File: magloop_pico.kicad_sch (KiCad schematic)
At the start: 102 parts, among them J1 Conn_Coaxial_Power, J10 5V AUDIO MUTE, J2 Conn_02x03_Odd_Even, J3 POWER SW, J4 Conn_02x03_Odd_Even, J5 Conn_02x04_Odd_Even, J6 TO RF RELAY, J7 ETHERNET, J8 5-1634513-1, J9 12V AUDIO MUTE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

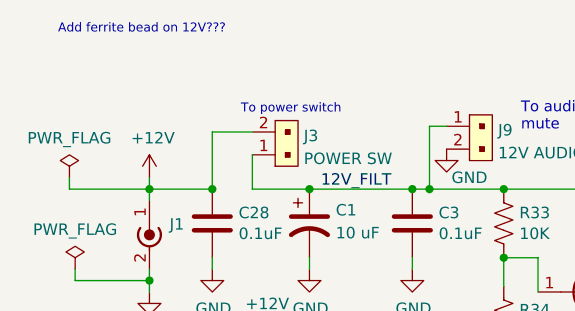
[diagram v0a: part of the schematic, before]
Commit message: Added BOM directory
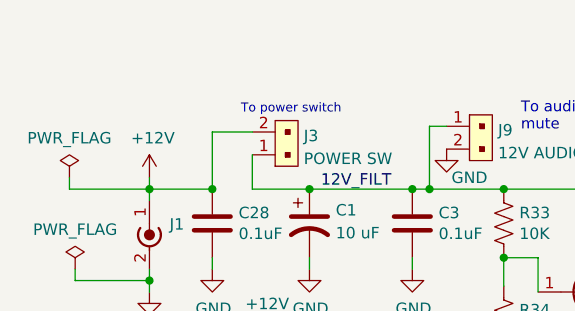
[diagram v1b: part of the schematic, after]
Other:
- note removed: "Add ferrite bead on 12V???"
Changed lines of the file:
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@@
     (effects (font (size 2.0066 2.0066)) (justify left bottom))
-  )
-  (text "Add ferrite bead on 12V???" (at 16.51 5.715 0)
-    (effects (font (size 1 1)) (justify left bottom))
   )
   (text "RF bypasses or ferrite beads for stepper outs?" (at 12.065 192.405 0)

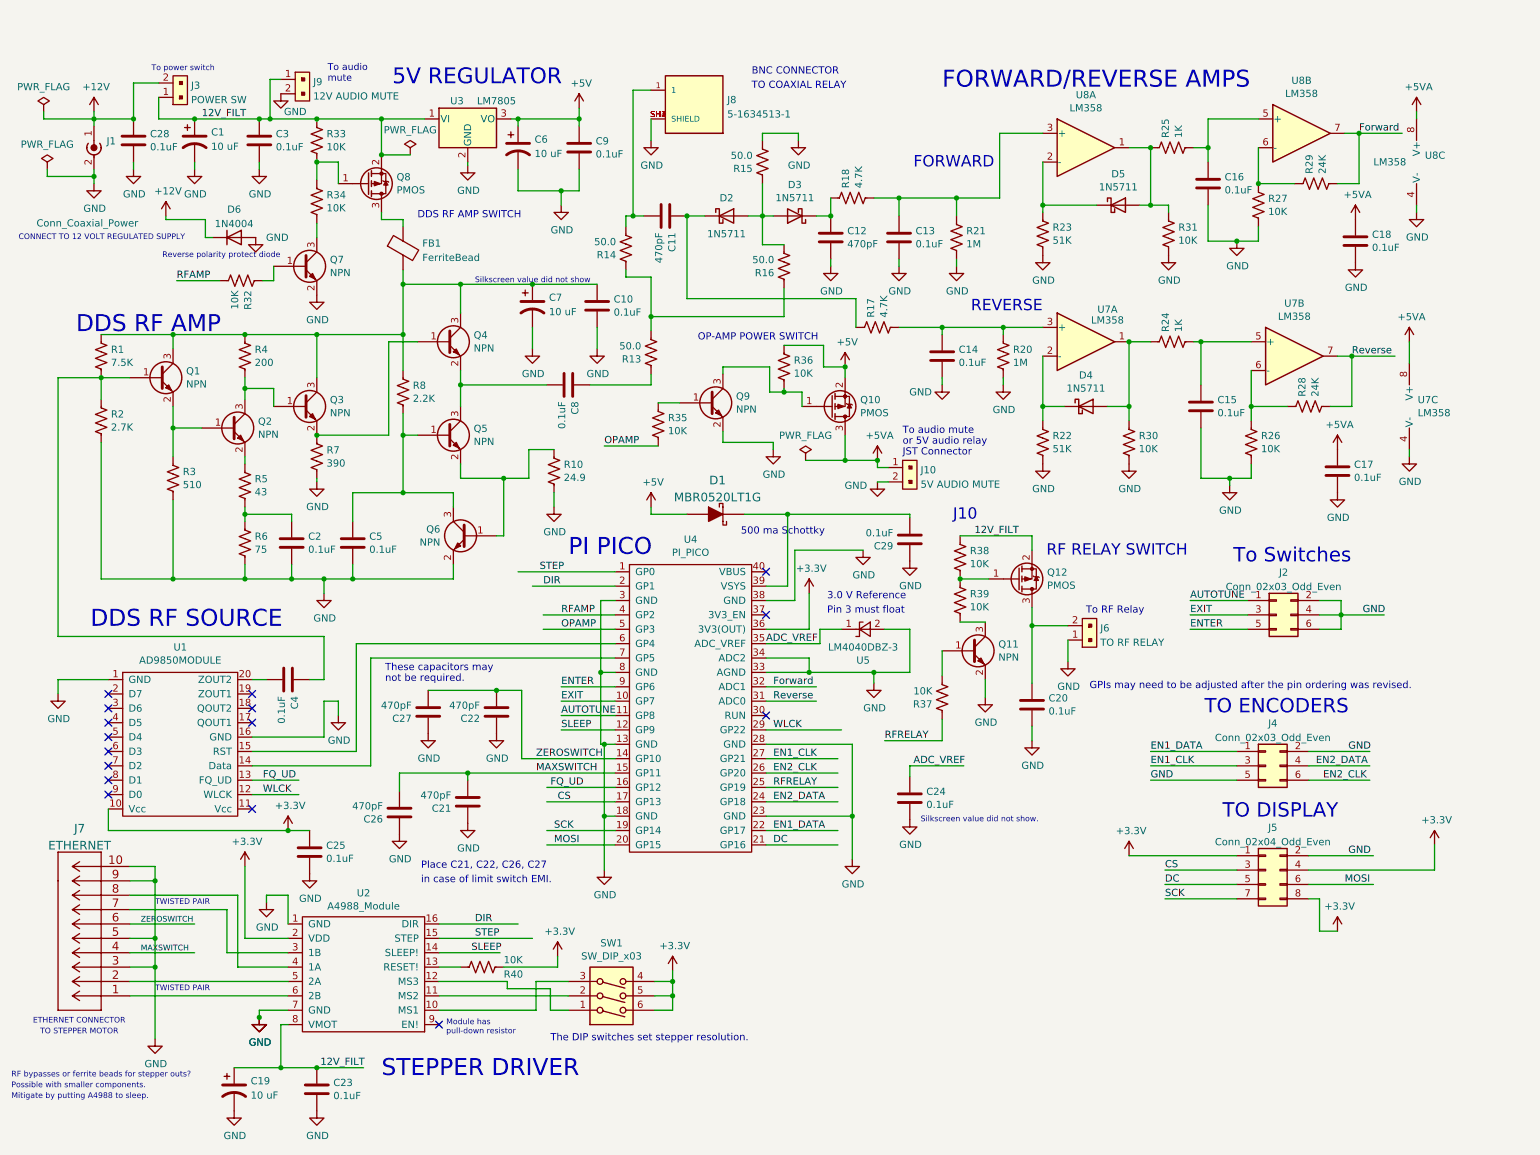
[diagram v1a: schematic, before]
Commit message: Added BOMs from Digikey and Kicad schematic.  Minor clean up top metal and changed 50 ohm resistors to 51.
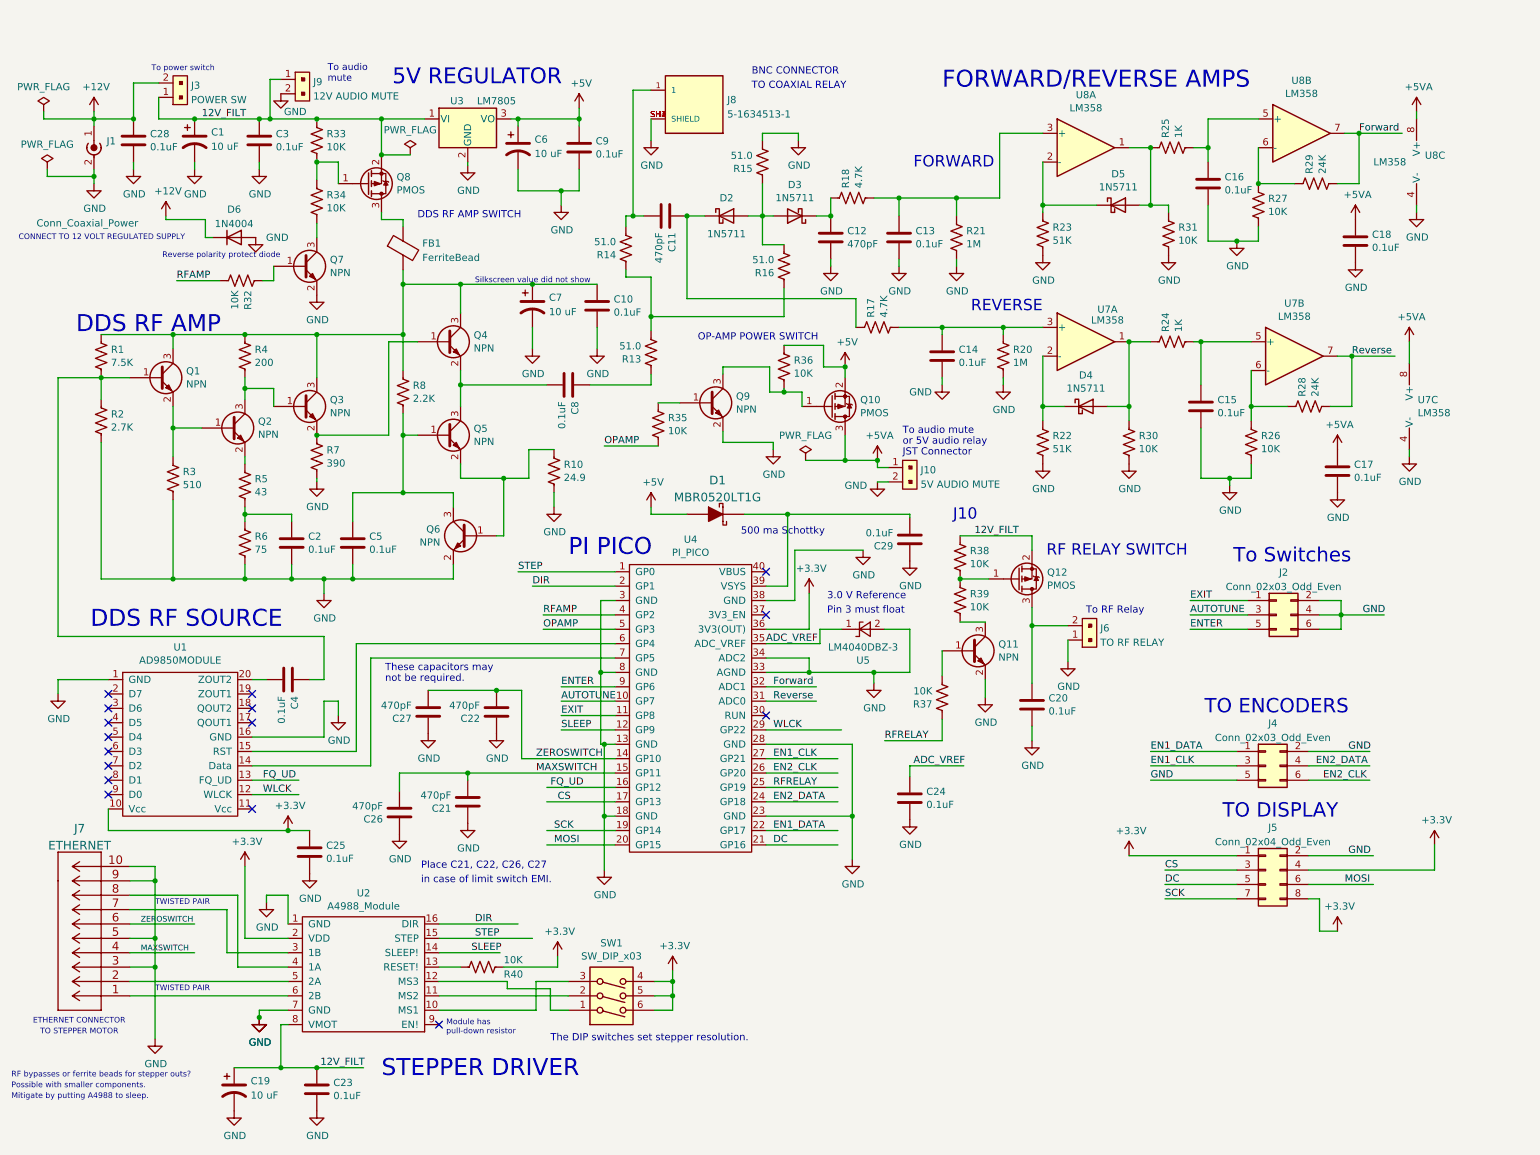
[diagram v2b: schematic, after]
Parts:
- R13, R14, R15, R16: value 50.0 -> 51.0
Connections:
- net AUTOTUNE: now also J2.3 (Pin_3), U4.10 (GP7); no longer J2.1 (Pin_1), U4.11 (GP8)
- net EXIT: now also J2.1 (Pin_1), U4.11 (GP8); no longer J2.3 (Pin_3), U4.10 (GP7)
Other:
- note removed: "GPIs may need to be adjusted after the pin ordering was revised."
- note removed: "Silkscreen value did not show."
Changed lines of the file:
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@@
     (effects (font (size 1.27 1.27)) (justify left bottom))
   )
-  (text "GPIs may need to be adjusted after the pin ordering was revised."
-    (at 202.565 123.825 0)
-    (effects (font (size 1.27 1.27)) (justify left bottom))
-  )
   (text "TWISTED PAIR" (at 37.465 177.165 0)
     (effects (font (size 0.9906 0.9906)) (justify left bottom))
@@
     (effects (font (size 1.27 1.27)) (justify left bottom))
   )
-  (text "Silkscreen value did not show." (at 172.72 147.32 0)
-    (effects (font (size 1 1)) (justify left bottom))
-  )
   (text "TO ENCODERS" (at 222.885 128.27 0)
     (effects (font (size 2.54 2.54)) (justify left bottom))
@@
     (effects (font (size 1.27 1.27)) (justify left bottom))
   )
-  (label "EXIT" (at 109.22 125.73 0)
+  (label "AUTOTUNE" (at 109.22 125.73 0)
     (effects (font (size 1.27 1.27)) (justify left bottom))
   )
@@
     (effects (font (size 1.27 1.27)) (justify left bottom))
   )
-  (label "AUTOTUNE" (at 109.22 128.27 0)
+  (label "EXIT" (at 109.22 128.27 0)
     (effects (font (size 1.27 1.27)) (justify left bottom))
   )
@@
     (effects (font (size 1.27 1.27)) (justify left bottom))
   )
-  (label "STEP" (at 105.41 102.87 0)
+  (label "STEP" (at 101.6 102.87 0)
     (effects (font (size 1.27 1.27)) (justify left bottom))
   )
@@
     (effects (font (size 1.27 1.27)) (justify left bottom))
   )
-  (label "EXIT" (at 220.345 110.49 0)
+  (label "AUTOTUNE" (at 220.345 110.49 0)
     (effects (font (size 1.27 1.27)) (justify left bottom))
   )
@@
     (effects (font (size 1.27 1.27)) (justify left bottom))
   )
-  (label "AUTOTUNE" (at 220.345 107.95 0)
+  (label "EXIT" (at 220.345 107.95 0)
     (effects (font (size 1.27 1.27)) (justify left bottom))
   )
@@
     (effects (font (size 1.27 1.27)) (justify left bottom))
   )
-  (label "RFAMP" (at 109.22 110.49 0)
+  (label "RFAMP" (at 106.045 110.49 0)
     (effects (font (size 1.27 1.27)) (justify left bottom))
   )
@@
     (effects (font (size 1.27 1.27)) (justify left bottom))
   )
-  (label "OPAMP" (at 109.22 113.03 0)
+  (label "OPAMP" (at 106.045 113.03 0)
     (effects (font (size 1.27 1.27)) (justify left bottom))
   )
@@
     (effects (font (size 1.27 1.27)) (justify left bottom))
   )
-  (label "DIR" (at 106.045 105.41 0)
+  (label "DIR" (at 104.14 105.41 0)
     (effects (font (size 1.27 1.27)) (justify left bottom))
   )
@@
       (effects (font (size 1.27 1.27)) (justify left))
     )
-    (property "Value" "50.0" (id 1) (at 123.3678 62.992 0)
+    (property "Value" "51.0" (id 1) (at 123.3678 62.992 0)
       (effects (font (size 1.27 1.27)) (justify left))
     )
@@
       (effects (font (size 1.27 1.27)) (justify left))
     )
-    (property "Value" "50.0" (id 1) (at 146.8628 47.752 0)
+    (property "Value" "51.0" (id 1) (at 146.8628 47.752 0)
       (effects (font (size 1.27 1.27)) (justify left))
     )
@@
       (effects (font (size 1.27 1.27)) (justify left))
     )
-    (property "Value" "50.0" (id 1) (at 143.0528 29.337 0)
+    (property "Value" "51.0" (id 1) (at 143.0528 29.337 0)
       (effects (font (size 1.27 1.27)) (justify left))
     )
@@
       (effects (font (size 1.27 1.27)) (justify left))
     )
-    (property "Value" "50.0" (id 1) (at 118.9228 44.577 0)
+    (property "Value" "51.0" (id 1) (at 118.9228 44.577 0)
       (effects (font (size 1.27 1.27)) (justify left))
     )
@@
     )
     (path "/00000000-0000-0000-0000-000060ee0403"
-      (reference "R13") (unit 1) (value "50.0") (footprint "Resistor_SMD:R_1206_3216Metric_Pad1.30x1.75mm_HandSolder")
+      (reference "R13") (unit 1) (value "51.0") (footprint "Resistor_SMD:R_1206_3216Metric_Pad1.30x1.75mm_HandSolder")
     )
     (path "/00000000-0000-0000-0000-000060ee422a"
-      (reference "R14") (unit 1) (value "50.0") (footprint "Resistor_SMD:R_1206_3216Metric_Pad1.30x1.75mm_HandSolder")
+      (reference "R14") (unit 1) (value "51.0") (footprint "Resistor_SMD:R_1206_3216Metric_Pad1.30x1.75mm_HandSolder")
     )
     (path "/00000000-0000-0000-0000-000060ee2682"
-      (reference "R15") (unit 1) (value "50.0") (footprint "Resistor_SMD:R_1206_3216Metric_Pad1.30x1.75mm_HandSolder")
+      (reference "R15") (unit 1) (value "51.0") (footprint "Resistor_SMD:R_1206_3216Metric_Pad1.30x1.75mm_HandSolder")
     )
     (path "/00000000-0000-0000-0000-000060ee12e0"
-      (reference "R16") (unit 1) (value "50.0") (footprint "Resistor_SMD:R_1206_3216Metric_Pad1.30x1.75mm_HandSolder")
+      (reference "R16") (unit 1) (value "51.0") (footprint "Resistor_SMD:R_1206_3216Metric_Pad1.30x1.75mm_HandSolder")
     )
     (path "/00000000-0000-0000-0000-000060f150a6"

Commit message: Released PCB 1.0
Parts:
- removed R40: 10K, Resistor_SMD:R_1206_3216Metric_Pad1.30x1.75mm_HandSolder, symbol Device:R_US
- removed U2: A4988_Module, magloop_pico:A4988_MODULE, symbol A4988_module:A4988_Module
- added R9: 0, Resistor_SMD:R_1206_3216Metric_Pad1.30x1.75mm_HandSolder, symbol Device:R_US
- added U2: TMC2209_Module, symbol A4988_module:TMC2209_Module
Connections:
- net SLEEP is gone; now on net EXIT: U4.12 (GP9)
- net +3V3: now also U2.2 (VDD)
- net 12V_FILT: now also U2.8 (VMOT)
- net DIR: now also U2.16 (DIR)
- net EXIT: no longer U4.11 (GP8)
- net GND: now also R9.1, U2.1 (GND), U2.7 (GND)
- net STEP: now also U2.15 (STEP)
- net at SW1.3: now also U2.10 (MS1)
- net at SW1.2: now also U2.11 (MS2)
- net at J7.7: now also U2.3 (1B)
- net at J7.8: now also U2.4 (1A)
- net at J7.2: now also U2.5 (2A)
- net at J7.1: now also U2.6 (2B)
- new net: R9.2, U2.9 (EN!)
- new net UART_TX: U2.13 (UART_RX), U4.11 (GP8)
- no-connect marks 16 -> 17
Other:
- note removed: "Module has pull-down resistor"
- title: Pi Pico Magnetic Loop Controller 1.0 -> Pi Pico Magnetic Loop Controller 2.0
